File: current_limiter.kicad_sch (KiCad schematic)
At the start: 23 parts, among them J401 Conn_02x02, Q401 MMBT5551, Q402 MMBT5551, Q403 LBSS84LT1G, U402 COS1333TR, U404 LMV321-TR

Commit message: Silkscreen mostly done
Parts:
- removed C408: 100nF, Capacitor_SMD:C_0402_1005Metric, symbol Device:C
- C409, C412: value 100nF -> 1uF; LCSC C1525 -> C52923
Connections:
- net FVSS: now also C409.1
- net GND: no longer C409.1
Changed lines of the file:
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@@
 	)
 	(junction
-		(at 100.33 80.01)
-		(diameter 0)
-		(color 0 0 0 0)
-	)
-	(junction
 		(at 59.69 97.79)
 		(diameter 0)
@@
 	(wire
 		(pts
-			(xy 100.33 80.01) (xy 105.41 80.01)
+			(xy 106.68 60.96) (xy 106.68 58.42)
 		)
 		(stroke
@@
 	(wire
 		(pts
-			(xy 100.33 80.01) (xy 100.33 83.82)
+			(xy 100.33 78.74) (xy 100.33 83.82)
 		)
 		(stroke
@@
 	(wire
 		(pts
-			(xy 100.33 80.01) (xy 100.33 78.74)
-		)
-		(stroke
-			(width 0)
-			(type default)
-		)
-	)
-	(wire
-		(pts
 			(xy 100.33 53.34) (xy 91.44 53.34)
 		)
@@
 		)
 	)
+	(label "FVSS"
+		(at 106.68 60.96 180)
+		(effects
+			(font
+				(size 1.27 1.27)
+			)
+			(justify right bottom)
+		)
+	)
 	(label "CCSC1"
 		(at 50.8 90.17 180)
@@
 	)
 	(symbol
-		(lib_id "power:GND")
-		(at 106.68 58.42 0)
-		(unit 1)
-		(exclude_from_sim no)
-		(in_bom yes)
-		(on_board yes)
-		(dnp no)
-		(property "Reference" "#PWR03603"
-			(at 106.68 64.77 0)
-			(effects
-				(font
-					(size 1.27 1.27)
-				)
-				(hide yes)
-			)
-		)
-		(property "Value" "GND"
-			(at 110.49 60.96 0)
-			(effects
-				(font
-					(size 1.27 1.27)
-				)
-			)
-		)
-		(property "Footprint" ""
-			(at 106.68 58.42 0)
-			(effects
-				(font
-					(size 1.27 1.27)
-				)
-				(hide yes)
-			)
-		)
-		(property "Datasheet" ""
-			(at 106.68 58.42 0)
-			(effects
-				(font
-					(size 1.27 1.27)
-				)
-				(hide yes)
-			)
-		)
-		(property "Description" "Power symbol creates a global label with name \"GND\" , ground"
-			(at 106.68 58.42 0)
-			(effects
-				(font
-					(size 1.27 1.27)
-				)
-				(hide yes)
-			)
-		)
-		(pin "1"
-		)
-		(instances
-			(project "HALPI2"
-				(path "/abc482bd-3f17-4d35-80db-1da3dcdb5c27/c7bf4e1f-6bd1-4be7-9e56-1bd438bf5d42/949897e8-9bb6-4c13-b9c6-3f831f2e4c69/ceedefa9-b0a1-435b-ac8f-bf0512726438"
-					(reference "#PWR03603")
-					(unit 1)
-				)
-			)
-		)
-	)
-	(symbol
 		(lib_id "Connector_Generic:Conn_02x02_Odd_Even")
 		(at 233.68 83.82 90)
@@
 			)
 		)
-		(property "Value" "100nF"
+		(property "Value" "1uF"
 			(at 152.4 74.93 90)
 			(effects
@@
 			)
 		)
-		(property "LCSC" "C1525"
+		(property "LCSC" "C52923"
 			(at 152.4 80.01 0)
 			(effects
@@
 	(symbol
 		(lib_id "power:GND")
-		(at 105.41 87.63 0)
-		(unit 1)
-		(exclude_from_sim no)
-		(in_bom yes)
-		(on_board yes)
-		(dnp no)
-		(property "Reference" "#PWR03602"
-			(at 105.41 93.98 0)
-			(effects
-				(font
-					(size 1.27 1.27)
-				)
-				(hide yes)
-			)
-		)
-		(property "Value" "GND"
-			(at 105.537 92.0242 0)
-			(effects
-				(font
-					(size 1.27 1.27)
-				)
-			)
-		)
-		(property "Footprint" ""
-			(at 105.41 87.63 0)
-			(effects
-				(font
-					(size 1.27 1.27)
-				)
-				(hide yes)
-			)
-		)
-		(property "Datasheet" ""
-			(at 105.41 87.63 0)
-			(effects
-				(font
-					(size 1.27 1.27)
-				)
-				(hide yes)
-			)
-		)
-		(property "Description" "Power symbol creates a global label with name \"GND\" , ground"
-			(at 105.41 87.63 0)
-			(effects
-				(font
-					(size 1.27 1.27)
-				)
-				(hide yes)
-			)
-		)
-		(pin "1"
-		)
-		(instances
-			(project "HALPI2"
-				(path "/abc482bd-3f17-4d35-80db-1da3dcdb5c27/c7bf4e1f-6bd1-4be7-9e56-1bd438bf5d42/949897e8-9bb6-4c13-b9c6-3f831f2e4c69/ceedefa9-b0a1-435b-ac8f-bf0512726438"
-					(reference "#PWR03602")
-					(unit 1)
-				)
-			)
-		)
-	)
-	(symbol
-		(lib_id "power:GND")
 		(at 128.27 105.41 0)
 		(unit 1)
@@
 	)
 	(symbol
-		(lib_id "Device:C")
-		(at 105.41 83.82 0)
-		(mirror x)
-		(unit 1)
-		(exclude_from_sim no)
-		(in_bom yes)
-		(on_board yes)
-		(dnp no)
-		(property "Reference" "C408"
-			(at 110.49 82.55 0)
-			(effects
-				(font
-					(size 1.27 1.27)
-				)
-			)
-		)
-		(property "Value" "100nF"
-			(at 111.76 85.09 0)
-			(effects
-				(font
-					(size 1.27 1.27)
-				)
-			)
-		)
-		(property "Footprint" "Capacitor_SMD:C_0402_1005Metric"
-			(at 106.3752 80.01 0)
-			(effects
-				(font
-					(size 1.27 1.27)
-				)
-				(hide yes)
-			)
-		)
-		(property "Datasheet" "~"
-			(at 105.41 83.82 0)
-			(effects
-				(font
-					(size 1.27 1.27)
-				)
-				(hide yes)
-			)
-		)
-		(property "Description" ""
-			(at 105.41 83.82 0)
-			(effects
-				(font
-					(size 1.27 1.27)
-				)
-				(hide yes)
-			)
-		)
-		(property "LCSC" "C1525"
-			(at 105.41 83.82 0)
-			(effects
-				(font
-					(size 1.27 1.27)
-				)
-				(hide yes)
-			)
-		)
-		(property "Characteristics" ""
-			(at 105.41 83.82 0)
-			(effects
-				(font
-					(size 1.27 1.27)
-				)
-				(hide yes)
-			)
-		)
-		(pin "1"
-		)
-		(pin "2"
-		)
-		(instances
-			(project "HALPI2"
-				(path "/abc482bd-3f17-4d35-80db-1da3dcdb5c27/c7bf4e1f-6bd1-4be7-9e56-1bd438bf5d42/949897e8-9bb6-4c13-b9c6-3f831f2e4c69/ceedefa9-b0a1-435b-ac8f-bf0512726438"
-					(reference "C408")
-					(unit 1)
-				)
-			)
-		)
-	)
-	(symbol
 		(lib_id "Device:R")
 		(at 50.8 80.01 0)
@@
 			)
 		)
-		(property "Value" "100nF"
+		(property "Value" "1uF"
 			(at 113.03 57.15 0)
 			(effects
@@
 			)
 		)
-		(property "LCSC" "C1525"
+		(property "LCSC" "C52923"
 			(at 106.68 55.88 0)
 			(effects

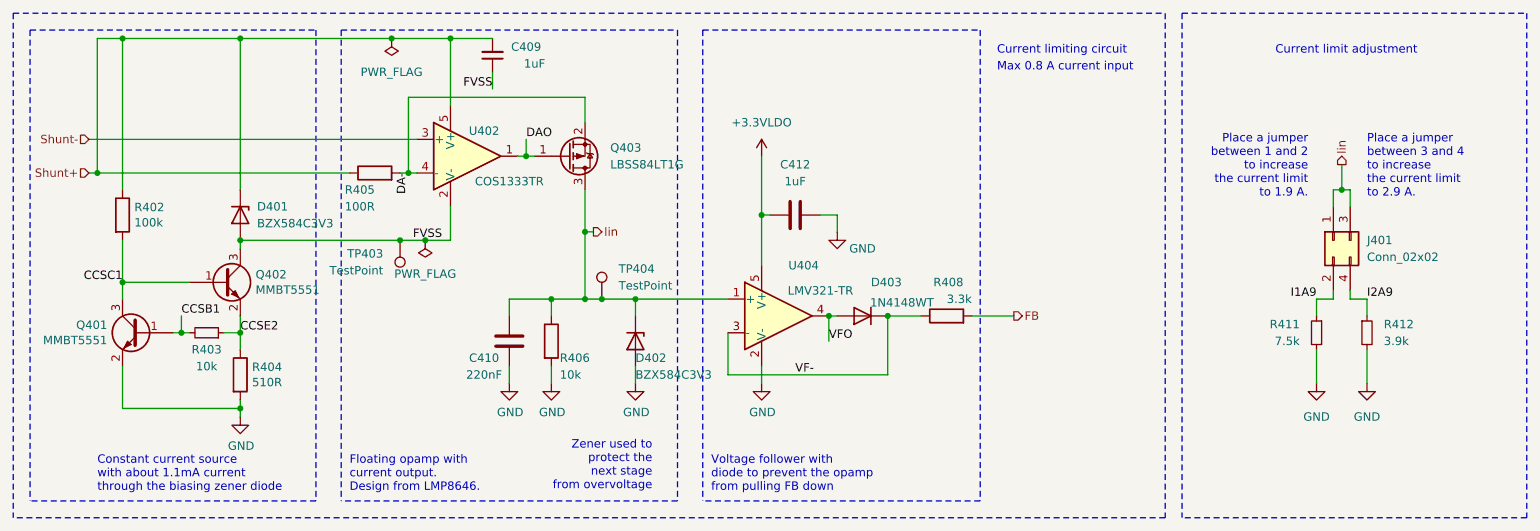
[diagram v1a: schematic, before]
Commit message: Finish the board redesign with SoM on the bottom
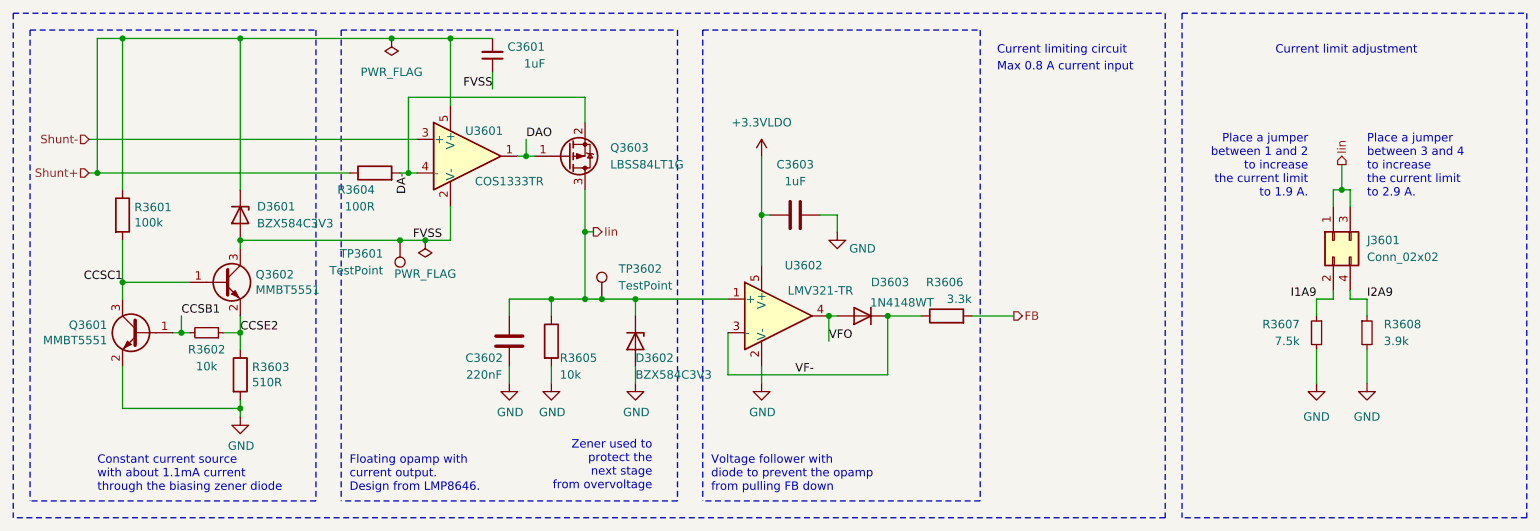
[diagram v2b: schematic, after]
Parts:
- renumbered C409 to C3601, C410 to C3602, C412 to C3603, D401 to D3601, D402 to D3602, D403 to D3603, J401 to J3601, Q401 to Q3601, Q402 to Q3602, Q403 to Q3603, R402 to R3601, R403 to R3602, R404 to R3603, R405 to R3604, R406 to R3605, R408 to R3606, R411 to R3607, R412 to R3608, TP403 to TP3601, TP404 to TP3602, U402 to U3601, U404 to U3602

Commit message: Further refinements
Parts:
- Q3602: Component Class fine_pitch -> (none)

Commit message: Change MCU to RP2040
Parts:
- J3601: footprint Connector_PinHeader_2.54mm:PinHeader_2x02_P2.54mm_Vertical -> Connector_PinHeader_2.54mm:PinHeader_2x02_P2.54mm_Vertical_SMD; LCSC C492419 -> C919361
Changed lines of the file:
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@@
 			)
 		)
-		(property "Footprint" "Connector_PinHeader_2.54mm:PinHeader_2x02_P2.54mm_Vertical"
+		(property "Footprint" "Connector_PinHeader_2.54mm:PinHeader_2x02_P2.54mm_Vertical_SMD"
 			(at 233.68 83.82 0)
 			(effects
@@
 			)
 		)
-		(property "LCSC" "C492419"
+		(property "LCSC" "C919361"
 			(at 233.68 83.82 90)
 			(effects

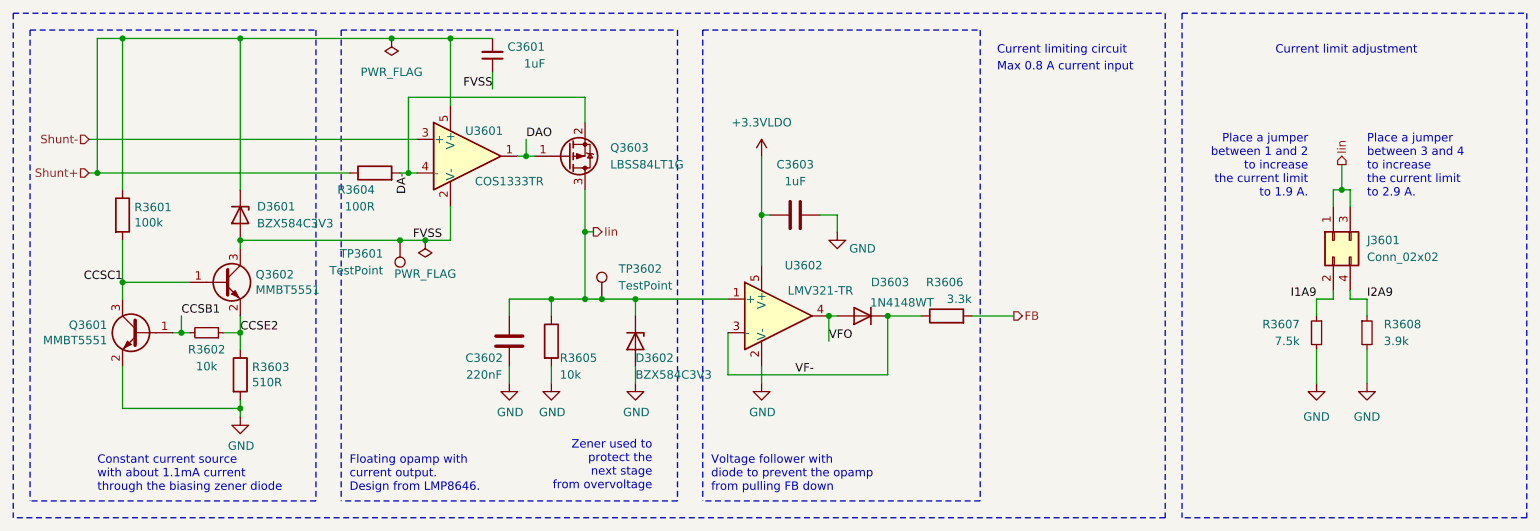
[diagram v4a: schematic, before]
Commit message: Finish transitioning to RP2040
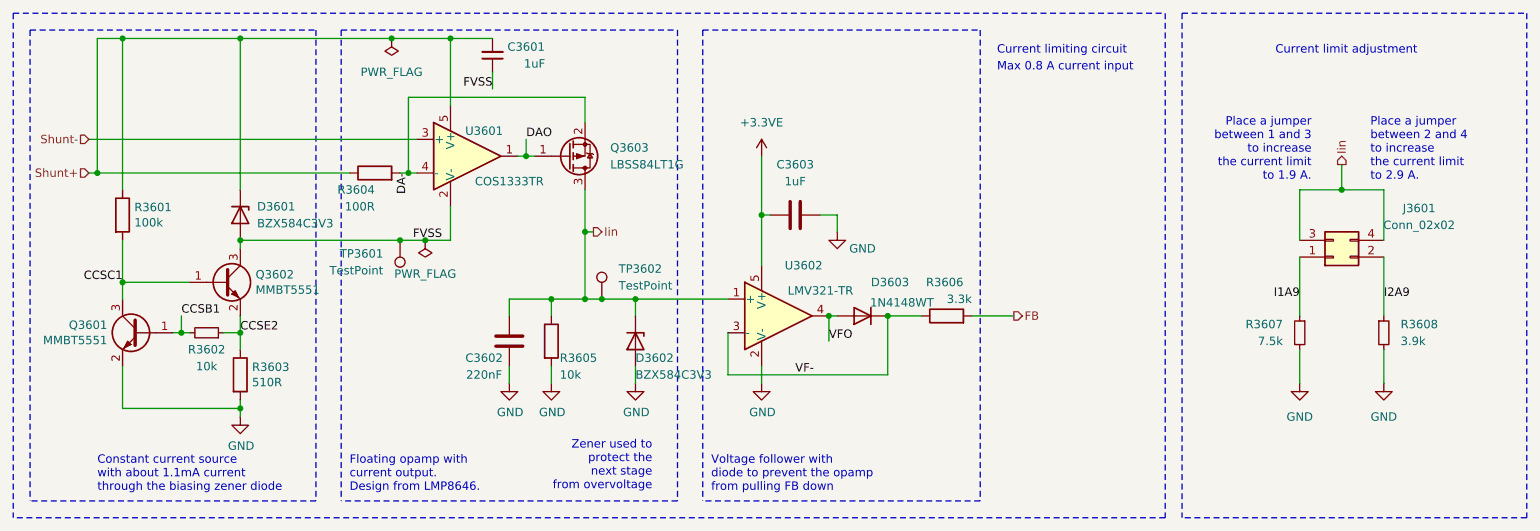
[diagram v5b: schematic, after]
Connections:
- net I1A9: now also J3601.1 (Pin_1); no longer J3601.2 (Pin_2)
- net I2A9: now also J3601.2 (Pin_2); no longer J3601.4 (Pin_4)
- net Iin: now also J3601.4 (Pin_4); no longer J3601.1 (Pin_1)
- net +3.3VLDO renamed +3.3VE
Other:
- note added: "Place a jumper between 1 and 3 to increase the current limit to 1.9 A."
- note added: "Place a jumper between 2 and 4 to increase the current limit to 2.9 A."
- note removed: "Place a jumper between 1 and 2 to increase the current limit to 1.9 A."
- note removed: "Place a jumper between 3 and 4 to increase the current limit to 2.9 A."
- moved on the sheet: J3601, R3607, R3608

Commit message: Apply part PCBA position corrections
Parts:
- J3601: JLCPCB_CORRECTION 1.27;1.27;90 -> 0;0;90
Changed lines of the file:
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@@
 			)
 		)
-		(property "JLCPCB_CORRECTION" "1.27;1.27;90"
+		(property "JLCPCB_CORRECTION" "0;0;90"
 			(at 233.68 86.36 0)
 			(effects
